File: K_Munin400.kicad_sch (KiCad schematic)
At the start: 87 parts, among them IC2 ACHS-7123-000E, J1 Conn_Coaxial, J19 To P.A., J2 Conn_Coaxial, J3 Conn_02x03_Odd_Even, J5 Wurth Redcube series, J6 Phoenix/1711725, Q1 MRF300AN, Q3 MRF300BN, Q4 BSS84, T1 Transformer_1P_1S, T2 FT-114A-61, T3 FT-114A-61, T4 FT-114A-61, U1 LM358, U2 LM78M05_TO252, U3 LMC660AIM_NOPB

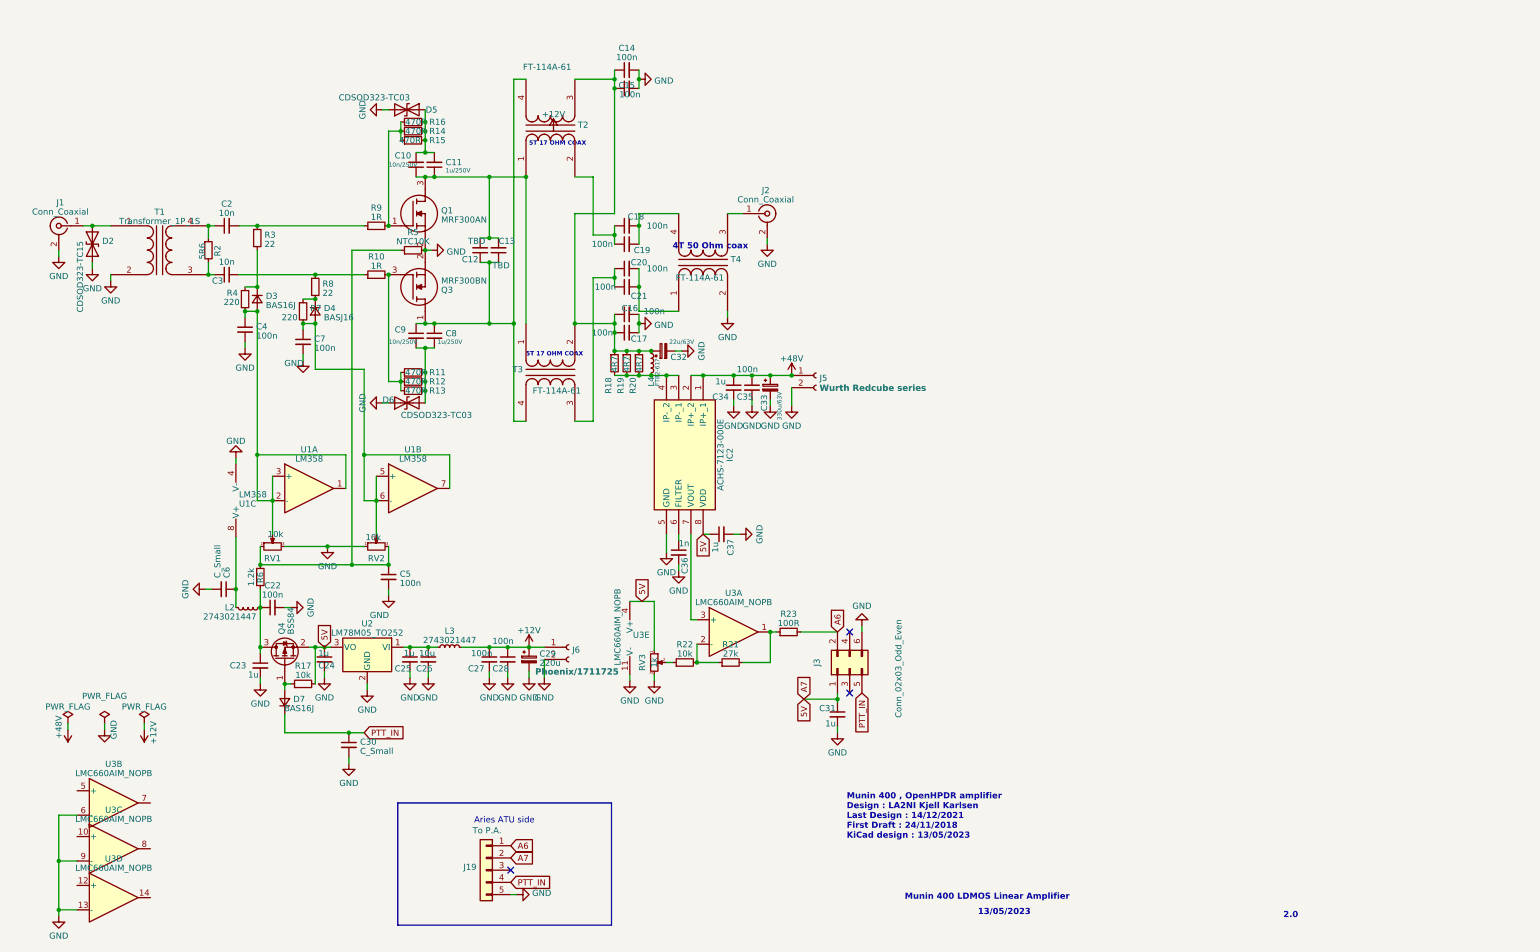
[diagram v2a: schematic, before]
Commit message: all footprint and 3D module defined, schematic completed
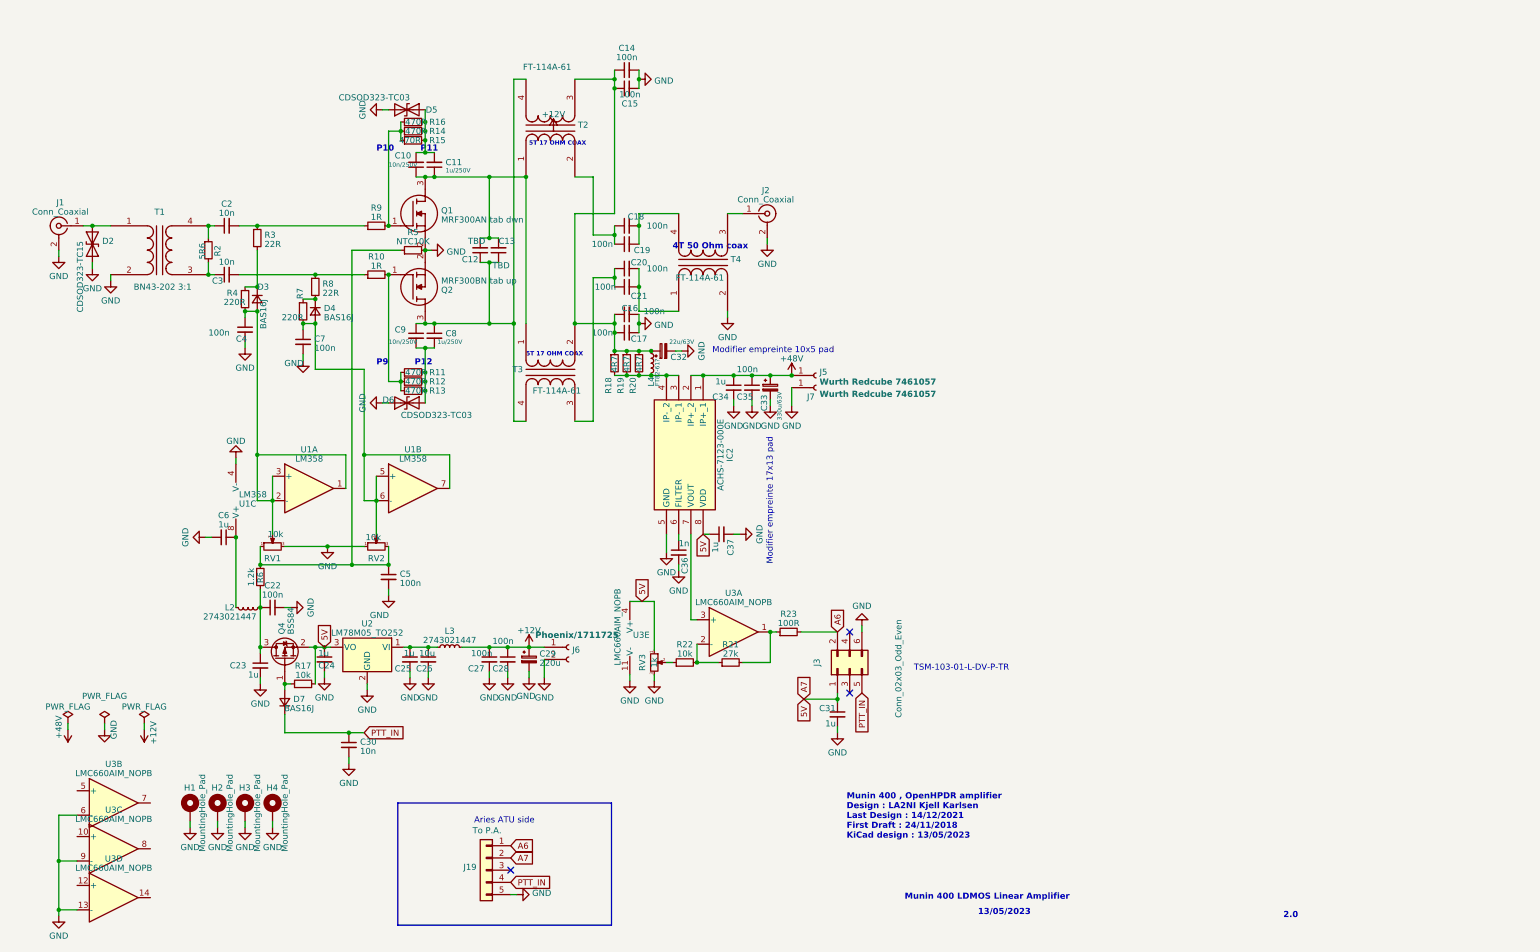
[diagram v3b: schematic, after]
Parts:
- removed J5: Wurth Redcube series, symbol Connector:Conn_01x02_Socket
- removed Q3: MRF300BN, TO544P521X1592X2551-3P, symbol MRF300BN:MRF300BN
- added H1, H2, H3, H4: MountingHole_Pad, MountingHole:MountingHole_3.5mm_Pad_TopBottom, symbol Mechanical:MountingHole_Pad
- added J5, J7: Wurth Redcube 7461057, 7461057:7461057, symbol Connector:Conn_01x01_Socket
- added Q2: MRF300BN tab up, MRF300BN:TO-247-3_Horizontal_TabUp, symbol MRF300AN:MRF300AN
- C10, C11, C12, C13, C14, C15, C16, C17, C18, C19, C20, C21, C8, C9: footprint (none) -> Capacitor_SMD:C_1812_4532Metric_Pad1.57x3.40mm_HandSolder
- C2, C22, C23, C24, C25, C27, C28, C3, C31, C34, C35, C36, C37, C4, C5, C7: footprint (none) -> Capacitor_SMD:C_0805_2012Metric_Pad1.18x1.45mm_HandSolder
- C26: footprint (none) -> Capacitor_Tantalum_SMD:CP_EIA-7343-31_Kemet-D_Pad2.25x2.55mm_HandSolder
- C29: footprint (none) -> Capacitor_SMD:C_Elec_8x10.2
- C30: value C_Small -> 10n; footprint (none) -> Capacitor_SMD:C_0805_2012Metric_Pad1.18x1.45mm_HandSolder
- C32: footprint (none) -> Capacitor_SMD:C_3640_9110Metric_Pad2.10x10.45mm_HandSolder
- C33: footprint (none) -> Capacitor_SMD:CP_Elec_18x17.5
- C6: value C_Small -> 1u; footprint (none) -> Capacitor_SMD:C_0805_2012Metric_Pad1.18x1.45mm_HandSolder
- D2, D5, D6: footprint Diode_THT:D_DO-201AE_P15.24mm_Horizontal -> Diode_SMD:D_SOD-323_HandSoldering
- D3, D7: footprint (none) -> Diode_SMD:D_SOD-323_HandSoldering
- D4: value BASJ16 -> BAS16J; footprint (none) -> Diode_SMD:D_SOD-323_HandSoldering
- J1, J2: footprint (none) -> SMA_PINS:SMA_PINS
- J3: footprint (none) -> Connector_PinHeader_2.54mm:PinHeader_2x03_P2.54mm_Vertical_SMD
- J6: footprint (none) -> 1711725:1711725
- L2, L3: footprint (none) -> Fair-Rite_2743021447:Fair-Rite_2743021447
- L4: footprint (none) -> T50:T50_V_smd
- Q1: value MRF300AN -> MRF300AN tab dwn; footprint TO544P521X1592X2551-3P -> MRF300AN:TO-247-3_Horizontal_TabDown
- R10, R17, R21, R22, R23, R5, R9: footprint (none) -> Resistor_SMD:R_0805_2012Metric_Pad1.20x1.40mm_HandSolder
- R11, R12, R13, R14, R15, R16: footprint (none) -> Resistor_THT:R_Axial_DIN0516_L15.5mm_D5.0mm_P30.48mm_Horizontal
- R18, R19, R2, R20: footprint (none) -> Resistor_SMD:R_1812_4532Metric_Pad1.30x3.40mm_HandSolder
- R3, R8: value 22 -> 22R; footprint (none) -> Resistor_SMD:R_0805_2012Metric_Pad1.20x1.40mm_HandSolder
- R4, R7: value 220 -> 220R; footprint (none) -> Resistor_SMD:R_0805_2012Metric_Pad1.20x1.40mm_HandSolder
- R6: footprint (none) -> Resistor_SMD:R_0815_2038Metric_Pad1.20x4.05mm_HandSolder
- RV1, RV2, RV3: footprint (none) -> Potentiometer_SMD:Potentiometer_Bourns_3269W_Vertical
- T1: value Transformer_1P_1S -> BN43-202 3:1; footprint (none) -> BN43-202-master:BN43-202
- T2, T3, T4: footprint (none) -> FT114A:FT114A-61
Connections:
- net +48V: now also J5.1 (Pin_1)
- net GND: now also H1.1, H2.1, H3.1, H4.1, J7.1 (Pin_1), Q2.2 (S)
- net at R10.2, R11.1, R12.1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: now also Q2.1 (G)
- net at C12.1, C13.1, C8.1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: now also Q2.3 (D)
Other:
- note added: "Modifier empreinte 10x5 pad"
- note added: "Modifier empreinte 17x13 pad"
- note added: "P10 P11"
- note added: "P9 P12"
- note added: "TSM-103-01-L-DV-P-TR"
- moved on the sheet: C6

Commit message: 3Dshapes set
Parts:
- IC2, U1: footprint Package_SO:SOIC-8_7.5x5.85mm_P1.27mm -> Package_SO:SOIC-8_3.9x4.9mm_P1.27mm
- R6: footprint Resistor_SMD:R_0815_2038Metric_Pad1.20x4.05mm_HandSolder -> Resistor_SMD:R_0805_2012Metric_Pad1.20x1.40mm_HandSolder
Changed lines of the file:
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@@
       (effects (font (size 1.27 1.27)))
     )
-    (property "Footprint" "Package_SO:SOIC-8_7.5x5.85mm_P1.27mm" (at 88.9 104.775 0)
+    (property "Footprint" "Package_SO:SOIC-8_3.9x4.9mm_P1.27mm" (at 88.9 104.775 0)
       (effects (font (size 1.27 1.27)) hide)
     )
@@
       (effects (font (size 1.27 1.27)) (justify left))
     )
-    (property "Footprint" "Package_SO:SOIC-8_7.5x5.85mm_P1.27mm" (at 54.61 107.315 0)
+    (property "Footprint" "Package_SO:SOIC-8_3.9x4.9mm_P1.27mm" (at 54.61 107.315 0)
       (effects (font (size 1.27 1.27)) hide)
     )
@@
       (effects (font (size 1.27 1.27)))
     )
-    (property "Footprint" "Package_SO:SOIC-8_7.5x5.85mm_P1.27mm" (at 67.31 104.775 0)
+    (property "Footprint" "Package_SO:SOIC-8_3.9x4.9mm_P1.27mm" (at 67.31 104.775 0)
       (effects (font (size 1.27 1.27)) hide)
     )
@@
       (effects (font (size 1.27 1.27)))
     )
-    (property "Footprint" "Package_SO:SOIC-8_7.5x5.85mm_P1.27mm" (at 54.305 110.49 0)
+    (property "Footprint" "Package_SO:SOIC-8_3.9x4.9mm_P1.27mm" (at 54.305 110.49 0)
       (effects (font (size 1.27 1.27)) (justify left top) hide)
     )
@@
       (effects (font (size 1.27 1.27)) (justify left))
     )
-    (property "Footprint" "Resistor_SMD:R_0815_2038Metric_Pad1.20x4.05mm_HandSolder" (at 57.15 123.19 0)
+    (property "Footprint" "Resistor_SMD:R_0805_2012Metric_Pad1.20x1.40mm_HandSolder" (at 57.15 123.19 0)
       (effects (font (size 1.27 1.27)) hide)
     )

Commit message: some debuging, new placement, silk logo
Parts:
- added H5: MountingHole_Pad, MountingHole:MountingHole_3.5mm_Pad_TopBottom, symbol Mechanical:MountingHole_Pad
- C32: footprint Capacitor_SMD:C_3640_9110Metric_Pad2.10x10.45mm_HandSolder -> Capacitor_SMD:C_2220_5650Metric_Pad1.97x5.40mm_HandSolder
- R5: footprint Resistor_SMD:R_0805_2012Metric_Pad1.20x1.40mm_HandSolder -> Resistor_SMD:R_MELF_MMB-0207
- T3: footprint FT114A:FT114A-61 -> FT114A:FT114A-61_B
- T4: footprint FT114A:FT114A-61 -> FT114A:FT114A-61_out
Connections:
- net GND: now also H5.1
- net at Q2.1 (G), R10.2, R11.1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: now also D6.1 (A1)
- net at C8.2, C9.2, R11.2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: no longer D6.1 (A1)
- net at Q1.1 (G), R14.1, R15.1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: now also D5.2 (A2)
- net at C10.1, C11.1, C12.2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: now also T2.3 (SB); no longer T2.1 (AA)
- net at C14.1, C15.1, C16.1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: now also T2.4 (SA), T3.4 (SA); no longer T2.3 (SA), T3.2 (AB)
- net at C10.2, C11.2, R14.2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: no longer D5.2 (A2)
- net at C20.1, C21.1: now also T3.2 (AB); no longer T3.3 (SA)
- net at C12.1, C13.1, C8.1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: now also T2.1 (AA), T3.3 (SB); no longer T2.4 (SB), T3.4 (SB)
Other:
- note added: "6T 8/10"
- note added: "C2220C226MMR2L7186 2022 Kemet"
- note added: "double empreinte sma/tnc?"
- note added: "option TNC pcb mount : 73204-5213 Molex tnc coudée 122440 amphenol TNC droite"
- note removed: "Modifier empreinte 10x5 pad"
- moved on the sheet: C14, C15, D5, D6

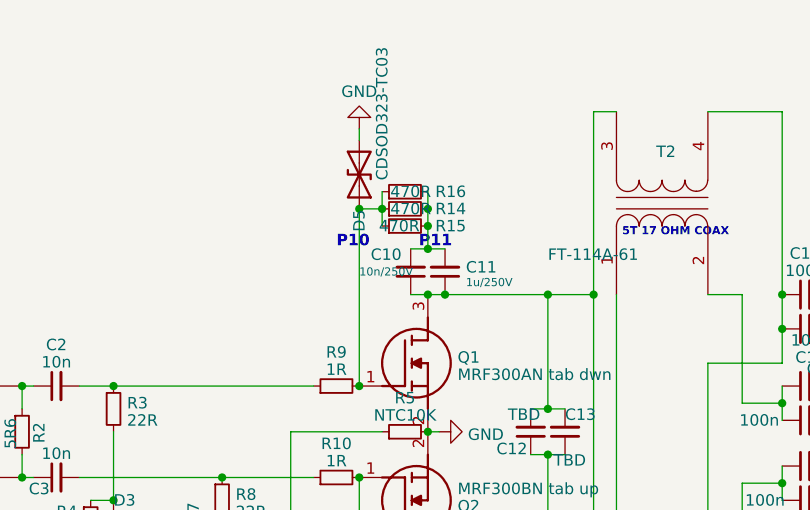
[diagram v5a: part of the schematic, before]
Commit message: placement and routing completed
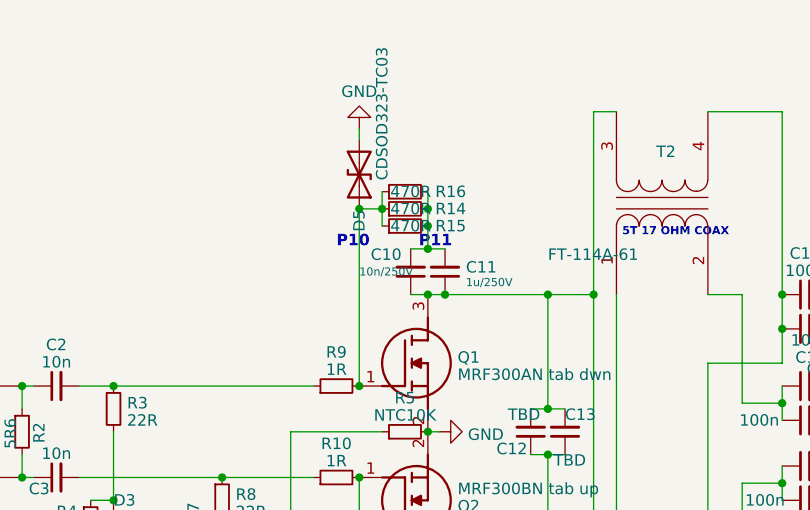
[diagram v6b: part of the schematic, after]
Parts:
- R11, R12, R13, R14, R15, R16: footprint Resistor_THT:R_Axial_DIN0516_L15.5mm_D5.0mm_P30.48mm_Horizontal -> Resistor_feedB:R_Axial_DIN0414_L11.9mm_D4.5mm_P25.40mm_Horizontal
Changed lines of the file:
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@@
       (effects (font (size 1.27 1.27)))
     )
-    (property "Footprint" "Resistor_THT:R_Axial_DIN0516_L15.5mm_D5.0mm_P30.48mm_Horizontal" (at 88.9 80.645 0)
+    (property "Footprint" "Resistor_feedB:R_Axial_DIN0414_L11.9mm_D4.5mm_P25.40mm_Horizontal" (at 88.9 80.645 0)
       (effects (font (size 1.27 1.27)) hide)
     )
@@
       (effects (font (size 1.27 1.27)))
     )
-    (property "Footprint" "Resistor_THT:R_Axial_DIN0516_L15.5mm_D5.0mm_P30.48mm_Horizontal" (at 88.9 84.455 0)
+    (property "Footprint" "Resistor_feedB:R_Axial_DIN0414_L11.9mm_D4.5mm_P25.40mm_Horizontal" (at 88.9 84.455 0)
       (effects (font (size 1.27 1.27)) hide)
     )
@@
       (effects (font (size 1.27 1.27)))
     )
-    (property "Footprint" "Resistor_THT:R_Axial_DIN0516_L15.5mm_D5.0mm_P30.48mm_Horizontal" (at 88.9 30.48 0)
+    (property "Footprint" "Resistor_feedB:R_Axial_DIN0414_L11.9mm_D4.5mm_P25.40mm_Horizontal" (at 88.9 30.48 0)
       (effects (font (size 1.27 1.27)) hide)
     )
@@
       (effects (font (size 1.27 1.27)))
     )
-    (property "Footprint" "Resistor_THT:R_Axial_DIN0516_L15.5mm_D5.0mm_P30.48mm_Horizontal" (at 88.9 82.55 0)
+    (property "Footprint" "Resistor_feedB:R_Axial_DIN0414_L11.9mm_D4.5mm_P25.40mm_Horizontal" (at 88.9 82.55 0)
       (effects (font (size 1.27 1.27)) hide)
     )
@@
       (effects (font (size 1.27 1.27)))
     )
-    (property "Value" "470R" (at 88.265 32.385 90)
+    (property "Value" "470R" (at 89.535 32.385 90)
       (effects (font (size 1.27 1.27)))
     )
-    (property "Footprint" "Resistor_THT:R_Axial_DIN0516_L15.5mm_D5.0mm_P30.48mm_Horizontal" (at 88.9 32.385 0)
+    (property "Footprint" "Resistor_feedB:R_Axial_DIN0414_L11.9mm_D4.5mm_P25.40mm_Horizontal" (at 88.9 32.385 0)
       (effects (font (size 1.27 1.27)) hide)
     )
@@
       (effects (font (size 1.27 1.27)))
     )
-    (property "Footprint" "Resistor_THT:R_Axial_DIN0516_L15.5mm_D5.0mm_P30.48mm_Horizontal" (at 88.9 28.575 0)
+    (property "Footprint" "Resistor_feedB:R_Axial_DIN0414_L11.9mm_D4.5mm_P25.40mm_Horizontal" (at 88.9 28.575 0)
       (effects (font (size 1.27 1.27)) hide)
     )
